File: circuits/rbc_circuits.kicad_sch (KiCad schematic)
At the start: 0 parts

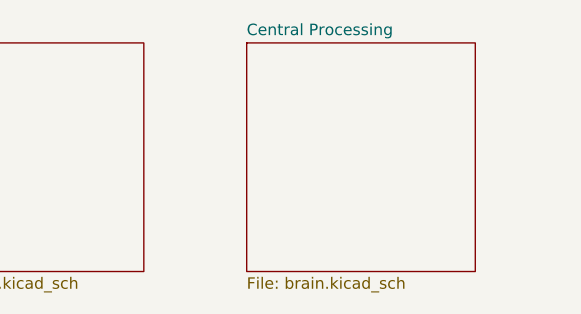
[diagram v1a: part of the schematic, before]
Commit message: motor shield circuit
BTN7030-1EPA
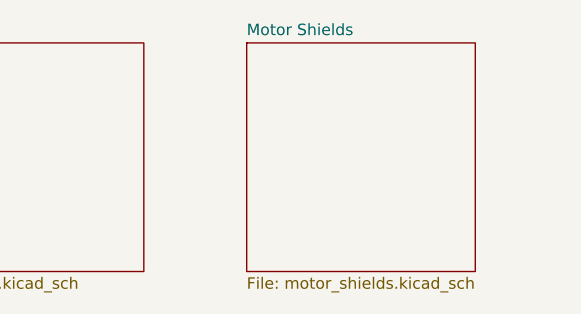
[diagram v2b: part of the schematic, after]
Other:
- sheet Central Processing renamed Motor Shields
- sheet Motor Shields: file brain.kicad_sch -> motor_shields.kicad_sch
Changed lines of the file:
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@@
     (stroke (width 0.1524) (type solid))
     (fill (color 0 0 0 0.0000))
-    (property "Sheetname" "Central Processing" (at 191.77 86.9184 0)
+    (property "Sheetname" "Motor Shields" (at 191.77 86.9184 0)
       (effects (font (size 1.27 1.27)) (justify left bottom))
     )
-    (property "Sheetfile" "brain.kicad_sch" (at 191.77 113.6146 0)
+    (property "Sheetfile" "motor_shields.kicad_sch" (at 191.77 113.6146 0)
       (effects (font (size 1.27 1.27)) (justify left top))
     )

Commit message: PCB Rev2.0 publish
It's here
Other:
- removed sheet Motor Controller
- added sheet MCU (MCU.kicad_sch)
- title: (none) -> RBC by UGS
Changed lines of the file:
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@@
 (kicad_sch (version 20230121) (generator eeschema)
   (paper "A4")
-  (sheet (at 116.84 87.63) (size 25.4 25.4) (fields_autoplaced)
-    (stroke (width 0.1524) (type solid))
-    (fill (color 0 0 0 0.0000))
-    (property "Sheetname" "Motor Controller" (at 116.84 86.9184 0)
-      (effects (font (size 1.27 1.27)) (justify left bottom))
-    )
-    (property "Sheetfile" "motor_controller.kicad_sch" (at 116.84 113.6146 0)
-      (effects (font (size 1.27 1.27)) (justify left top))
-    )
-    (instances
-      (project "rbc_circuits"
-        (path "/1df96114-eb1a-4ddf-9ea3-acd2b4d12bf3" (page "3"))
-      )
-    )
+  (title_block
+    (title "RBC by UGS")
+    (date "2023-09-06")
+    (rev "2.0")
   )
   (sheet (at 154.94 87.63) (size 25.4 25.4) (fields_autoplaced)
@@
       )
     )
+  )
+  (sheet (at 116.84 87.63) (size 24.13 25.4) (fields_autoplaced)
+    (stroke (width 0.1524) (type solid))
+    (fill (color 0 0 0 0.0000))
+    (property "Sheetname" "MCU" (at 116.84 86.9184 0)
+      (effects (font (size 1.27 1.27)) (justify left bottom))
+    )
+    (property "Sheetfile" "MCU.kicad_sch" (at 116.84 113.6146 0)
+      (effects (font (size 1.27 1.27)) (justify left top))
+    )
+    (instances
+      (project "rbc_circuits"
+        (path "/1df96114-eb1a-4ddf-9ea3-acd2b4d12bf3" (page "3"))
+      )
+    )
